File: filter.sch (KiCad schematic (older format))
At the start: 69 parts, among them J10 CV2, J8 QCV, J9 CV1, Q1 BC858, Q2 BC858, Q3 BC858, U2 LM13700, U5 TL074, U6 TL074, U7 TL074, U8 LM13700

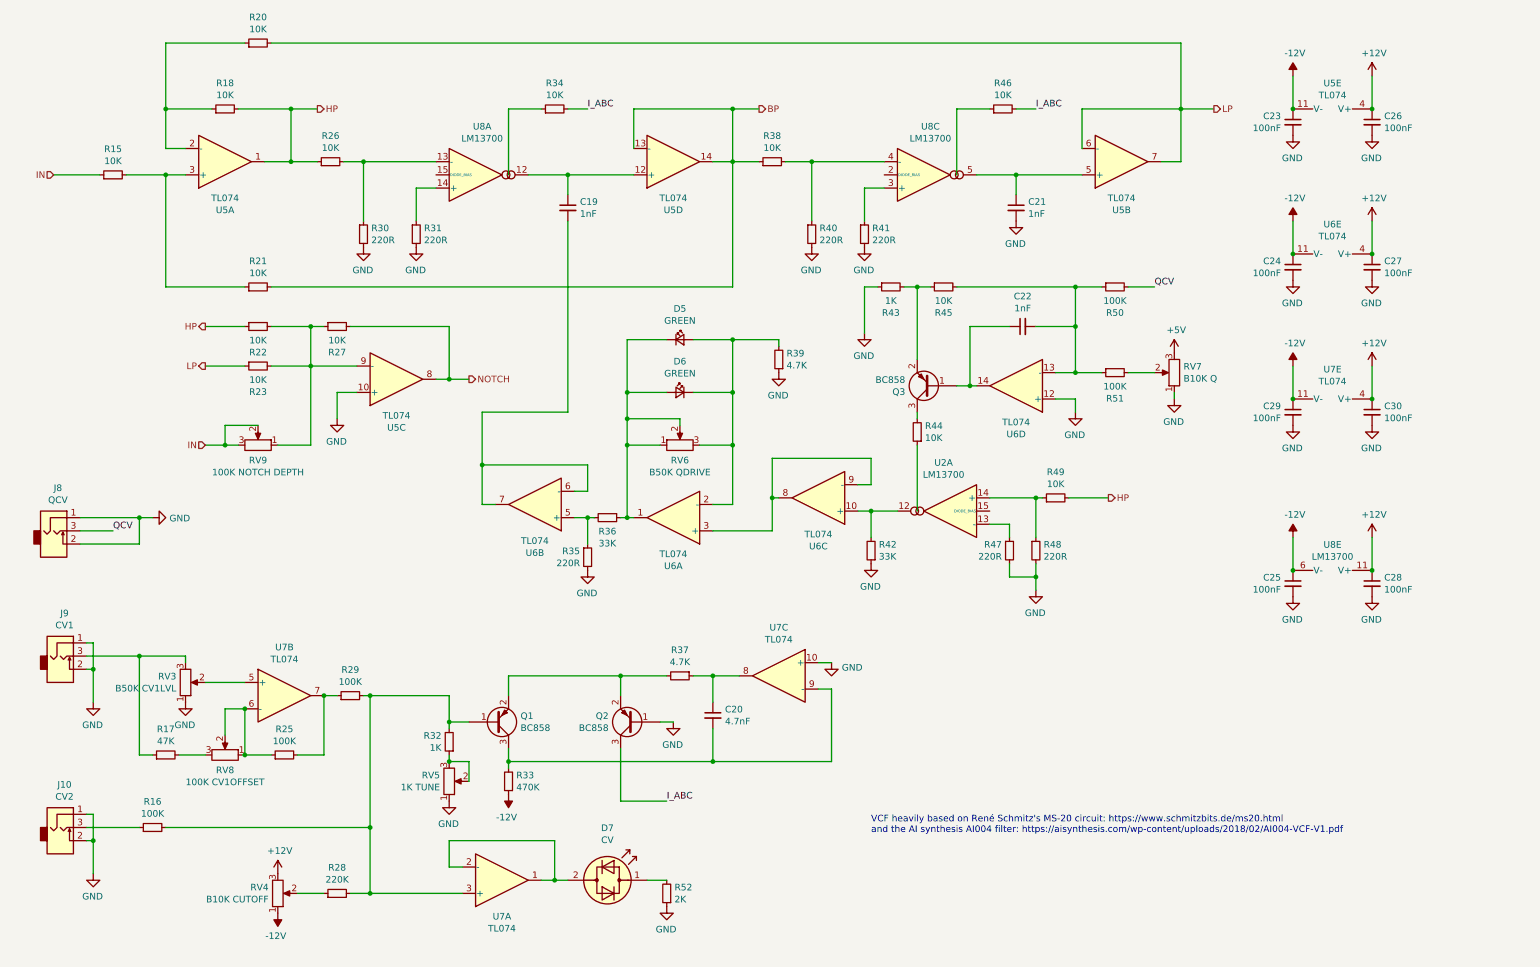
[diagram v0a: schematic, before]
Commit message: Update schematic with resonance and crossfader fixes
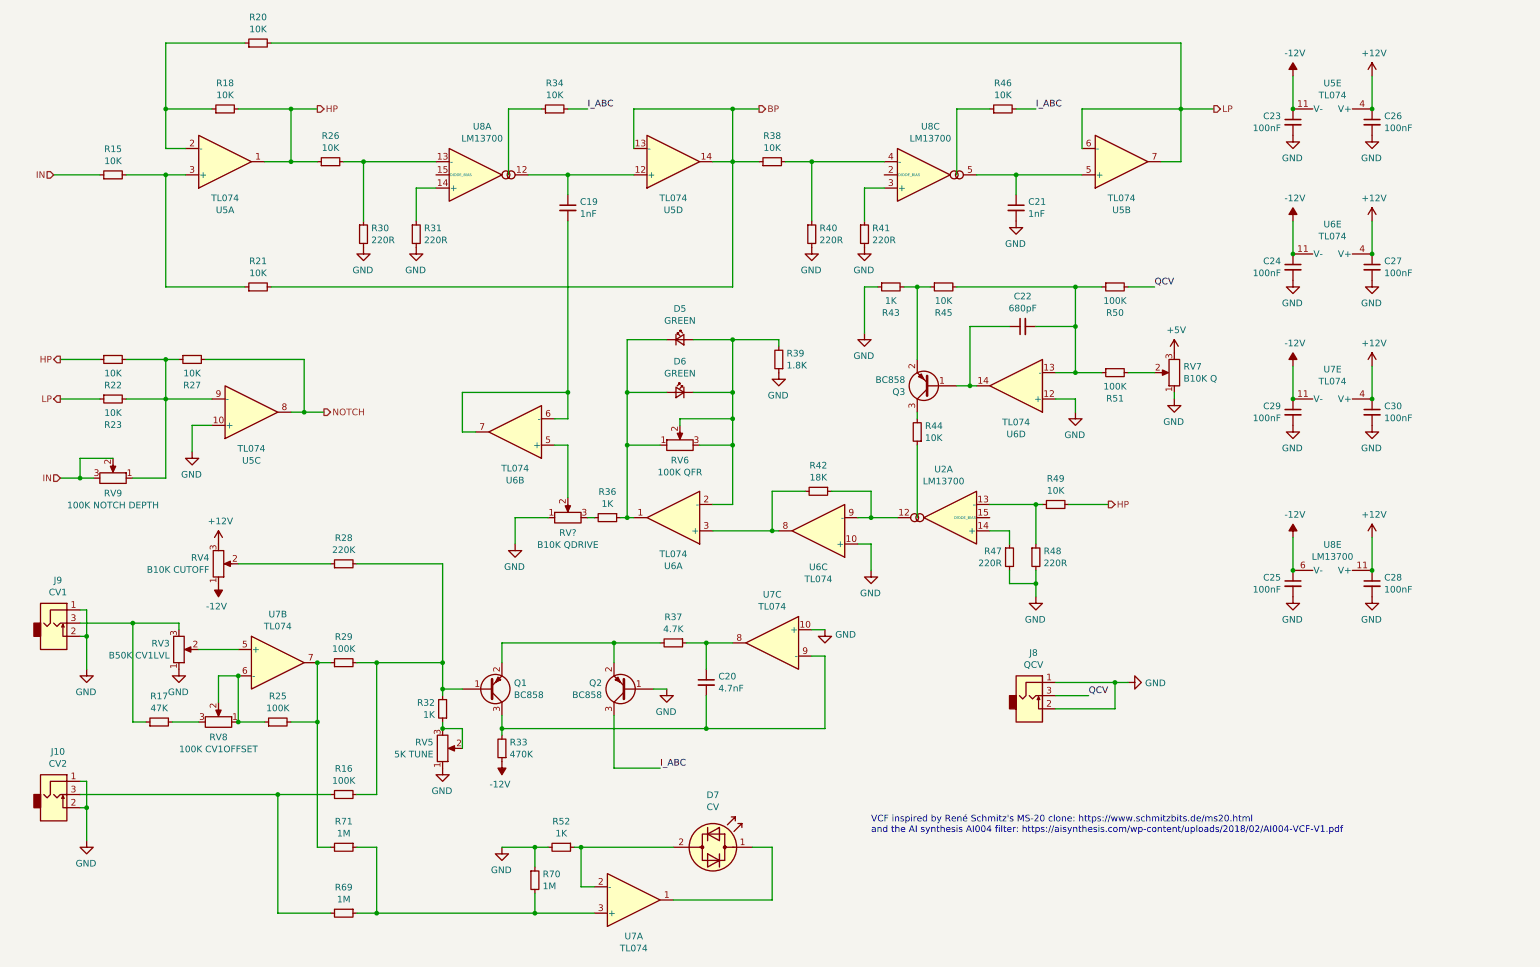
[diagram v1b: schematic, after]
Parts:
- removed R35: 220R, Resistor_SMD:R_0603_1608Metric, symbol Device:R_Small
- added R69, R70, R71: 1M, Resistor_SMD:R_0603_1608Metric, symbol Device:R_Small
- added RV?: B10K QDRIVE, Potentiometer_SMD:Potentiometer_Bourns_TC33X_Vertical, symbol Device:R_POT
- C22: value 1nF -> 680pF
- R36: value 33K -> 1K
- R39: value 4.7K -> 1.8K
- R42: value 33K -> 18K
- R52: value 2K -> 1K
- RV5: value 1K TUNE -> 5K TUNE
- RV6: value B50K QDRIVE -> 100K QFR
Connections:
- net GND: now also R52.2, U6.10 (+), R70.1, RV?.1; no longer R42.1, R52.1
- net at U2.13 (-): now also R48.1, R49.1; no longer R47.1
- net at U6.3 (+), U6.8: now also R42.2; no longer U6.9 (-)
- net at U6.5 (+): now also RV?.2; no longer R36.2
- net at D5.1 (K), D6.2 (A), R36.1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: no longer RV6.2
- net at D7.1 (KA): now also U7.1; no longer R52.2
- net at D7.2 (AK), U7.2 (-): now also R52.1; no longer U7.1
- net at Q1.1 (B), R16.2, R28.2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: no longer U7.3 (+)
- net at J10.3, R16.1: now also R69.2
- net at R25.2, R29.1, U7.7: now also R71.2
- net at D5.2 (A), D6.1 (K), R39.2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: now also RV6.2
- new net: R42.1, U2.12, U6.9 (-)
- new net: R47.1, U2.14 (+)
- new net: R36.2, RV?.3
- new net: R69.1, R70.2, R71.1, U7.3 (+)
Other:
- note added: "VCF inspired by René Schmitz's MS-20 clone: https://www.schmitzbits.de/ms20.html\nand the AI synthesis AI004 filter: https://aisynthesis.com/wp-content/uploads/2018/02/AI004-VCF-V1.pdf"
- note removed: "VCF heavily based on René Schmitz's MS-20 circuit: https://www.schmitzbits.de/ms20.html\nand the AI synthesis AI004 filter: https://aisynthesis.com/wp-content/uploads/2018/02/AI004-VCF-V1.pdf"
- moved on the sheet: C20, D7, J10, J8, J9, Q1, Q2, R16, R17, R22, R23, R25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

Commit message: Redesign filter core and revise board layout
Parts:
- removed R22, R23, R27: 10K, Resistor_SMD:R_0603_1608Metric, symbol Device:R_Small
- removed R36: 1K, Resistor_SMD:R_0603_1608Metric, symbol Device:R_Small
- removed RV9: 100K NOTCH DEPTH, Potentiometer_SMD:Potentiometer_Bourns_TC33X_Vertical, symbol Device:R_POT
- removed unit 3 of U5
- removed unit 2 of U6
- added C13: 1nF, Capacitor_SMD:C_0603_1608Metric, symbol Device:C_Small
- added C17: 0.47uF, Capacitor_SMD:C_0603_1608Metric, symbol Device:C_Small
- added C18, C19, C22, C23: 100nF, Capacitor_SMD:C_0603_1608Metric, symbol Device:C_Small
- added R21, R24, R28: 10K, Resistor_SMD:R_0603_1608Metric, symbol Device:R_Small
- added R31, R32: 220R, Resistor_SMD:R_0603_1608Metric, symbol Device:R_Small
- added unit 4 of U5
- added unit 3 of U7
- added unit 5 of U7
- added unit 3 of U9
- R35: renamed from R42; value 18K -> 10K
- RV5: renamed from RV?; value B10K QDRIVE -> B50K QDRIVE
- U10, U9: renamed from U7; value TL074 -> TL072; footprint Package_SO:TSSOP-14_4.4x5mm_P0.65mm -> Package_SO:TSSOP-8_4.4x3mm_P0.65mm; symbol Amplifier_Operational:TL074 -> Amplifier_Operational:TL072
- U8, U9: renamed from U6; value TL074 -> TL072; footprint Package_SO:TSSOP-14_4.4x5mm_P0.65mm -> Package_SO:TSSOP-8_4.4x3mm_P0.65mm; symbol Amplifier_Operational:TL074 -> Amplifier_Operational:TL072
- renumbered C21 to C12, C19 to C14, C23 to C15, C26 to C16, C24 to C20, C27 to C21, C29 to C24, C30 to C25, C20 to C26, C22 to C27, C25 to C28, C28 to C29, R18 to R20, R15 to R22, R46 to R23, R34 to R25, R38 to R27, R41 to R29, R40 to R30, R30 to R33, R31 to R34, R39 to R36, R20 to R37, R21 to R38, R44 to R39, R49 to R40, R48 to R41, R47 to R42, R37 to R43, R50 to R44, R43 to R46, R28 to R47, R32 to R48, R51 to R49, R33 to R50, R29 to R51, R17 to R52, R25 to R53, R71 to R54, R52 to R55, R16 to R56, R70 to R57, R69 to R58, RV8 to RV10, RV6 to RV4, RV4 to RV6, RV5 to RV8, RV3 to RV9, U8 to U6, U2 to U7
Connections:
- net +12V: now also U10.8 (V+), U8.8 (V+), C19.1, C23.1, U7.11 (V+), U9.8 (V+); no longer U10.4 (V+), U8.4 (V+)
- net -12V: now also U10.4 (V-), U8.4 (V-), C18.1, C22.1, U7.6 (V-), U9.4 (V-); no longer U10.11 (V-), U8.11 (V-)
- net BP: now also R21.2, U5.13 (-), U5.14; no longer R27.1, R38.2, U5.13 (-), U5.14
- net GND: now also U10.3 (+), U5.3 (+), U8.3 (+), U9.3 (+), C13.2, C18.2, C19.2, C22.2, C23.2, R31.2, R32.2; no longer RV5.1, U10.10 (+), U8.10 (+), U9.12 (+)
- net HP: now also R35.2, R28.1; no longer R20.2, R26.1, R40.2
- net IN: now also R26.1, R38.1; no longer R22.1
- net I_ABC: now also R24.2
- net at R25.1: now also U6.1; no longer U6.16
- net at R26.2, R33.1: now also R22.1, U6.4 (-); no longer U6.13 (-)
- net at R34.1: now also U6.3 (+); no longer U6.14 (+)
- net at C14.2: now also D5.1 (K), D6.2 (A), RV4.1, U8.7
- net at R23.1: now also U6.16; no longer U6.1
- net at R29.1: now also R27.2, U6.14 (+); no longer U6.3 (+)
- net at U7.16: now also R39.2; no longer R39.1
- net at C27.2, R44.1, R45.2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: now also U9.2 (-); no longer U9.13 (-)
- net at C27.1, Q3.1 (B): now also U9.1; no longer U9.14
- net I_RES: now reaches Q3.3 (C)
- net I_RES: now also R39.1; no longer R39.2
- net at RV5.2: now also RV5.3, U8.1, U8.5 (+)
- net at D7.2 (AK), R55.1: now also U9.6 (-); no longer U9.2 (-)
- net at D7.1 (KA): now also U9.7; no longer U9.1
- net at R54.1, R57.2, R58.1: now also U9.5 (+); no longer U9.3 (+)
- net at C26.1, R43.1: now also U10.1; no longer U10.8
- net at C26.2, Q1.3 (C), R50.2: now also U10.2 (-); no longer U10.9 (-)
- net at D5.2 (A), D6.1 (K), R36.2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: now also U8.6 (-); no longer U8.2 (-)
- removed net LP: R37.2, U5.6 (-), U5.7
- new net: R20.1, R30.1, U6.13 (-)
- new net: R35.1, R37.2, R38.2, U5.2 (-)
- new net: C14.1, U5.5 (+), U6.5
- new net: R22.2, R27.1, U5.6 (-), U5.7
- new net: C12.1, U5.10 (+), U6.12
- new net: RV5.1, U7.12, U8.2 (-)
- new net: C17.2, R40.2
- new net: R28.2, R31.1, U7.3 (+)
- new net: R24.1, U7.1
- new net: R21.1, R32.1, U7.4 (-)
- new net: C13.1, U5.12 (+), U7.5
- new net LP2: C17.1, R20.2, R37.1, U5.8, U5.9 (-)
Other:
- moved on the sheet: C12, C14, C15, C16, C20, C21, C24, C25, C26, C27, C28, C29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

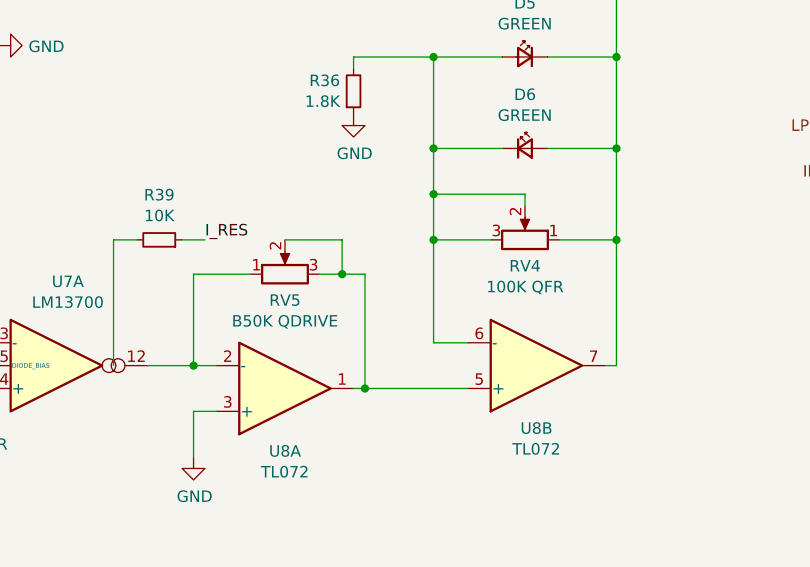
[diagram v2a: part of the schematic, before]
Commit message: Add panel, plus some minor fixes to crossfade and resonance drive
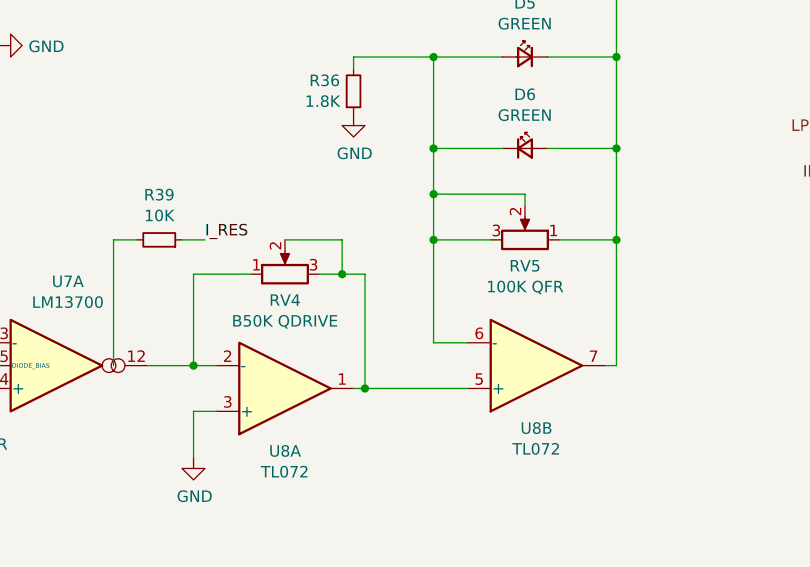
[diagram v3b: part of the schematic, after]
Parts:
- RV4: value 100K QFR -> B50K QDRIVE
- RV5: value B50K QDRIVE -> 100K QFR
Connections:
- net at C14.2, D5.1 (K), D6.2 (A)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: now also RV5.1; no longer RV4.1
- net at U7.12, U8.2 (-): now also RV4.1; no longer RV5.1
- net at U8.1, U8.5 (+): now also RV4.2, RV4.3; no longer RV5.2, RV5.3
- net at D5.2 (A), D6.1 (K), R36.2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: now also RV5.2, RV5.3; no longer RV4.2, RV4.3
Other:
- moved on the sheet: RV4, RV5
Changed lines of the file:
@@
 	2350 4500 2450 4500
 Connection ~ 3100 4400
-$Comp
-L Device:R_POT RV?
-U 1 1 601C6795
-P 2750 3900
-AR Path="/601C6795" Ref="RV?"  Part="1"
-AR Path="/613FC7FE/601C6795" Ref="RV5"  Part="1"
-F 0 "RV5" V 2635 3900 50  0000 C CNN
-F 1 "B50K QDRIVE" V 2544 3900 50  0000 C CNN
-F 2 "Potentiometer_SMD:Potentiometer_Bourns_TC33X_Vertical" V 2680 3900 50  0001 C CNN
-F 3 "~" H 2750 3900 50  0001 C CNN
-	1    2750 3900
-	0    -1   -1   0
-$EndComp
 Wire Wire Line
 	2000 3750 2000 4300
@@
 L Device:R_POT RV?
 U 1 1 615278C6
-P 3800 3750
+P 2750 3900
 AR Path="/615278C6" Ref="RV?"  Part="1"
 AR Path="/613FC7FE/615278C6" Ref="RV4"  Part="1"
-F 0 "RV4" V 3685 3750 50  0000 C CNN
-F 1 "100K QFR" V 3594 3750 50  0000 C CNN
-F 2 "SamacSys_Parts:Potentiometer_Alpha_RD901F-40-00D_Single_Vertical" H 3800 3750 50  0001 C CNN
-F 3 "~" H 3800 3750 50  0001 C CNN
-	1    3800 3750
-	0    1    -1   0
+F 0 "RV4" V 2635 3900 50  0000 C CNN
+F 1 "B50K QDRIVE" V 2544 3900 50  0000 C CNN
+F 2 "SamacSys_Parts:Potentiometer_Alpha_RD901F-40-00D_Single_Vertical" H 2750 3900 50  0001 C CNN
+F 3 "~" H 2750 3900 50  0001 C CNN
+	1    2750 3900
+	0    -1   -1   0
 $EndComp
 Wire Wire Line
@@
 Text HLabel 5150 3250 0    50   Output ~ 0
 LP2
+$Comp
+L Device:R_POT RV?
+U 1 1 601C6795
+P 3800 3750
+AR Path="/601C6795" Ref="RV?"  Part="1"
+AR Path="/613FC7FE/601C6795" Ref="RV5"  Part="1"
+F 0 "RV5" V 3685 3750 50  0000 C CNN
+F 1 "100K QFR" V 3594 3750 50  0000 C CNN
+F 2 "Potentiometer_SMD:Potentiometer_Bourns_TC33X_Vertical" V 3730 3750 50  0001 C CNN
+F 3 "~" H 3800 3750 50  0001 C CNN
+	1    3800 3750
+	0    1    -1   0
+$EndComp
 $EndSCHEMATC
